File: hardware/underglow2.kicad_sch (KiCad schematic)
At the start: 1 part, among them J101 J_Delphi_Sicma_24

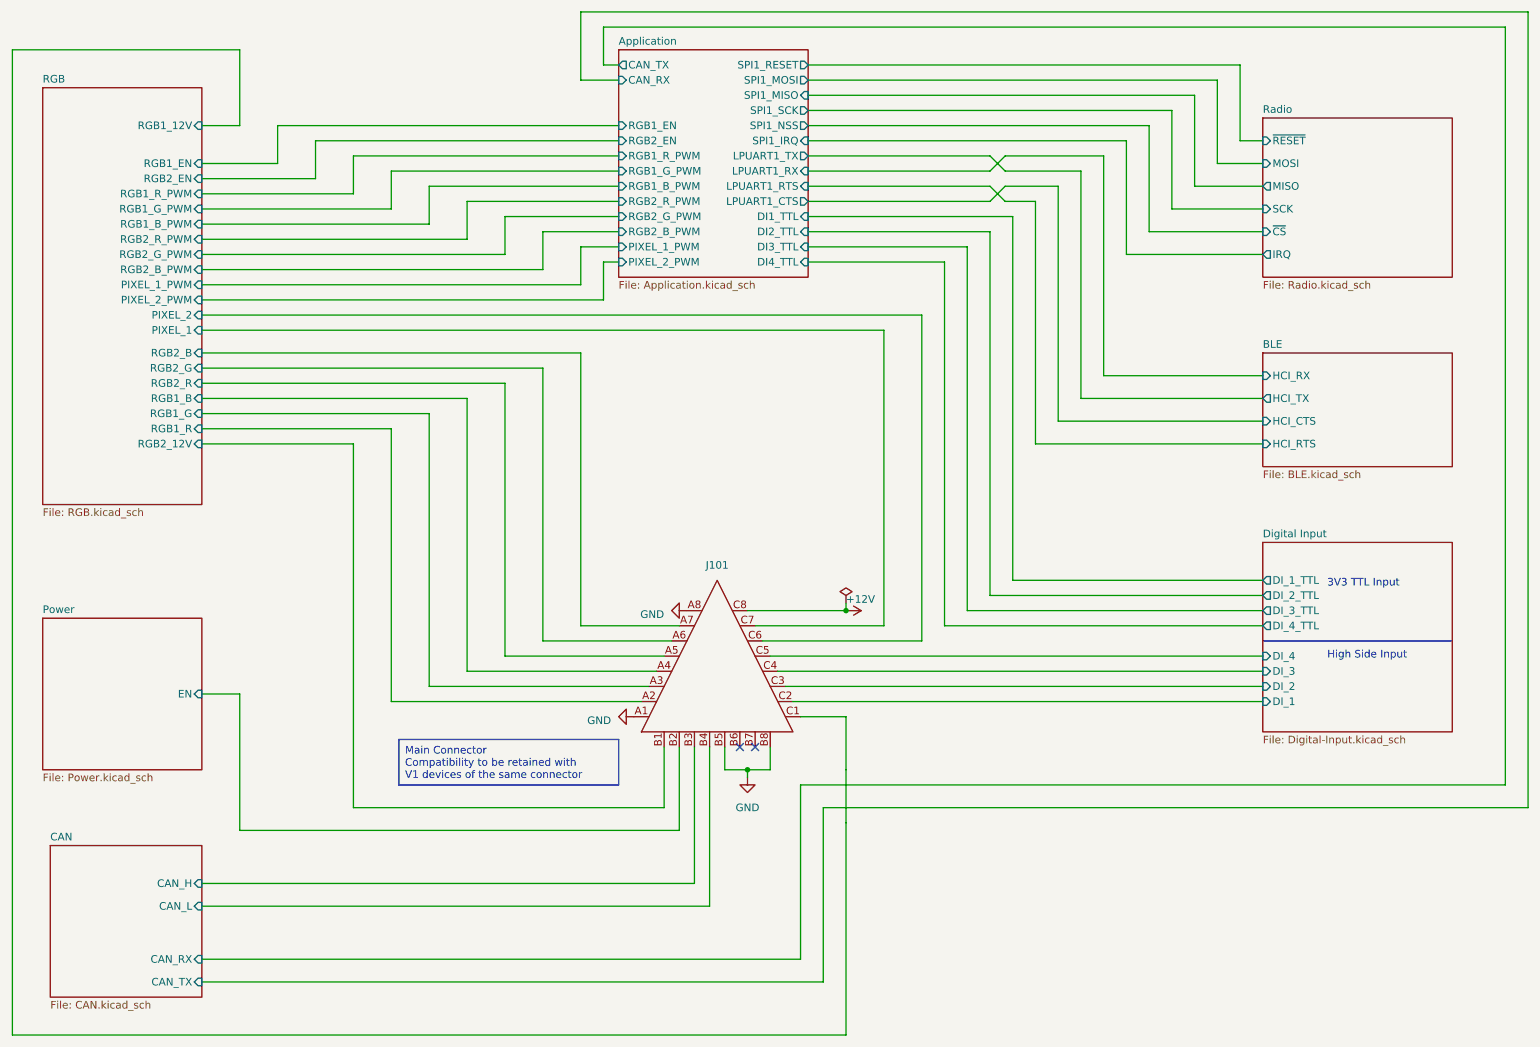
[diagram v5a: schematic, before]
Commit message: More pre-production updates:
* fix USART connections being reversed
* add test points for SPI and BLE

Signed-off-by: Connor Rigby <connorr@hey.com>
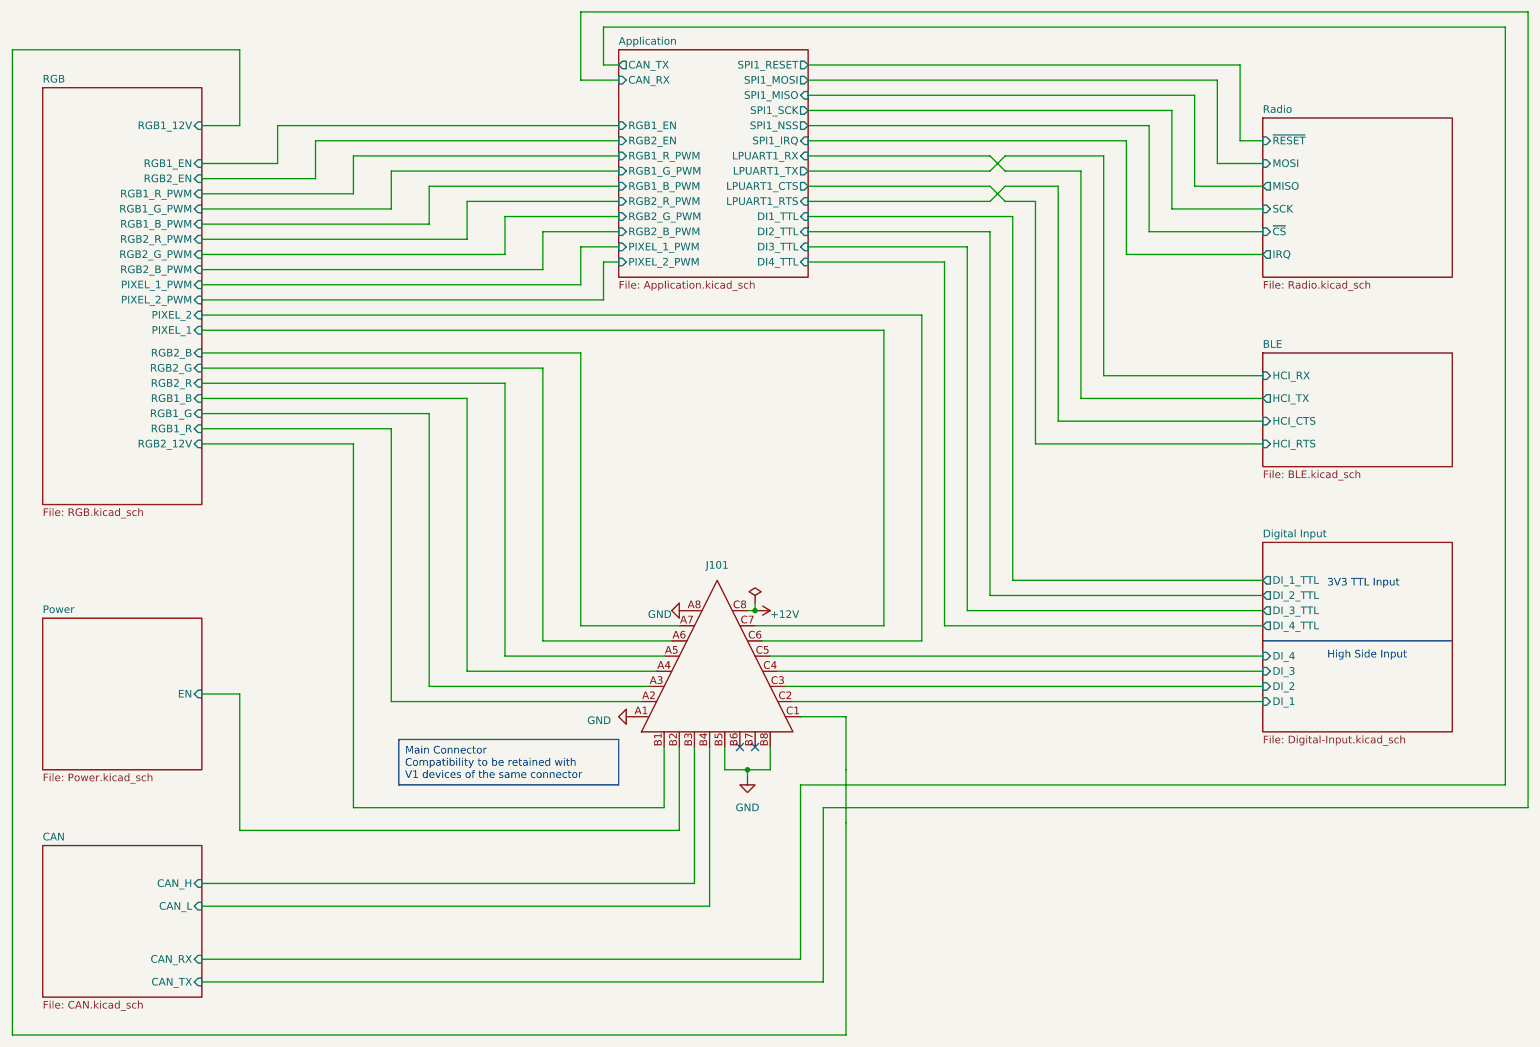
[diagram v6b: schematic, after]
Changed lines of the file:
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@@
   (junction (at 148.59 146.05) (diameter 0) (color 0 0 0 0)
   )
-  (junction (at 165.1 119.38) (diameter 0) (color 0 0 0 0)
+  (junction (at 149.86 119.38) (diameter 0) (color 0 0 0 0)
   )
   (no_connect (at 147.32 142.24))
@@
     (stroke (width 0) (type default))
   )
+  (wire (pts (xy 149.86 119.38) (xy 148.59 119.38))
+    (stroke (width 0) (type default))
+  )
   (wire (pts (xy 204.47 45.72) (xy 204.47 83.82))
     (stroke (width 0) (type default))
@@
     (stroke (width 0) (type default))
   )
-  (wire (pts (xy 165.1 118.11) (xy 165.1 119.38))
+  (wire (pts (xy 149.86 118.11) (xy 149.86 119.38))
     (stroke (width 0) (type default))
   )
@@
   )
   (wire (pts (xy 63.5 133.35) (xy 63.5 156.21))
-    (stroke (width 0) (type default))
-  )
-  (wire (pts (xy 165.1 119.38) (xy 148.59 119.38))
     (stroke (width 0) (type default))
   )
@@
   )
   (symbol (lib_id "power:GND") (at 138.43 119.38 270) (unit 1)
-    (in_bom yes) (on_board yes) (dnp no) (fields_autoplaced)
+    (in_bom yes) (on_board yes) (dnp no)
     (property "Reference" "#PWR0159" (at 132.08 119.38 0)
       (effects (font (size 1.27 1.27)) hide)
     )
-    (property "Value" "GND" (at 134.62 120.015 90)
+    (property "Value" "GND" (at 135.89 120.015 90)
       (effects (font (size 1.27 1.27)) (justify right))
     )
@@
     )
   )
-  (symbol (lib_id "power:PWR_FLAG") (at 165.1 118.11 0) (unit 1)
+  (symbol (lib_id "power:PWR_FLAG") (at 149.86 118.11 0) (unit 1)
     (in_bom yes) (on_board yes) (dnp no)
-    (property "Reference" "#FLG0105" (at 165.1 116.205 0)
-      (effects (font (size 1.27 1.27)) hide)
-    )
-    (property "Value" "PWR_FLAG" (at 165.1 114.3 0)
-      (effects (font (size 1.27 1.27)) hide)
-    )
-    (property "Footprint" "" (at 165.1 118.11 0)
-      (effects (font (size 1.27 1.27)) hide)
-    )
-    (property "Datasheet" "~" (at 165.1 118.11 0)
+    (property "Reference" "#FLG0105" (at 149.86 116.205 0)
+      (effects (font (size 1.27 1.27)) hide)
+    )
+    (property "Value" "PWR_FLAG" (at 149.86 114.3 0)
+      (effects (font (size 1.27 1.27)) hide)
+    )
+    (property "Footprint" "" (at 149.86 118.11 0)
+      (effects (font (size 1.27 1.27)) hide)
+    )
+    (property "Datasheet" "~" (at 149.86 118.11 0)
       (effects (font (size 1.27 1.27)) hide)
     )
@@
     )
   )
-  (symbol (lib_id "power:+12V") (at 165.1 119.38 270) (unit 1)
-    (in_bom yes) (on_board yes) (dnp no) (fields_autoplaced)
-    (property "Reference" "#PWR0107" (at 161.29 119.38 0)
-      (effects (font (size 1.27 1.27)) hide)
-    )
-    (property "Value" "+12V" (at 165.1 117.475 90)
-      (effects (font (size 1.27 1.27)) (justify left))
-    )
-    (property "Footprint" "" (at 165.1 119.38 0)
-      (effects (font (size 1.27 1.27)) hide)
-    )
-    (property "Datasheet" "" (at 165.1 119.38 0)
+  (symbol (lib_id "power:+12V") (at 149.86 119.38 270) (unit 1)
+    (in_bom yes) (on_board yes) (dnp no)
+    (property "Reference" "#PWR0107" (at 146.05 119.38 0)
+      (effects (font (size 1.27 1.27)) hide)
+    )
+    (property "Value" "+12V" (at 152.4 120.015 90)
+      (effects (font (size 1.27 1.27)) (justify left))
+    )
+    (property "Footprint" "" (at 149.86 119.38 0)
+      (effects (font (size 1.27 1.27)) hide)
+    )
+    (property "Datasheet" "" (at 149.86 119.38 0)
       (effects (font (size 1.27 1.27)) hide)
     )
@@
     )
   )
-  (sheet (at 31.75 158.75) (size 25.4 25.4) (fields_autoplaced)
+  (sheet (at 30.48 158.75) (size 26.67 25.4) (fields_autoplaced)
     (stroke (width 0.1524) (type solid))
     (fill (color 0 0 0 0.0000))
-    (property "Sheetname" "CAN" (at 31.75 158.0384 0)
+    (property "Sheetname" "CAN" (at 30.48 158.0384 0)
       (effects (font (size 1.27 1.27)) (justify left bottom))
     )
-    (property "Sheetfile" "CAN.kicad_sch" (at 31.75 184.7346 0)
+    (property "Sheetfile" "CAN.kicad_sch" (at 30.48 184.7346 0)
       (effects (font (size 1.27 1.27)) (justify left top))
     )
@@
       (effects (font (size 1.27 1.27)) (justify left))
     )
-    (pin "LPUART1_TX" output (at 158.75 43.18 0)
-      (effects (font (size 1.27 1.27)) (justify right))
-    )
-    (pin "LPUART1_RX" input (at 158.75 45.72 0)
-      (effects (font (size 1.27 1.27)) (justify right))
-    )
-    (pin "LPUART1_RTS" input (at 158.75 48.26 0)
-      (effects (font (size 1.27 1.27)) (justify right))
-    )
-    (pin "LPUART1_CTS" output (at 158.75 50.8 0)
-      (effects (font (size 1.27 1.27)) (justify right))
-    )
+    (pin "LPUART1_TX" output (at 158.75 45.72 0)
+      (effects (font (size 1.27 1.27)) (justify right))
+    )
+    (pin "LPUART1_RX" input (at 158.75 43.18 0)
+      (effects (font (size 1.27 1.27)) (justify right))
+    )
+    (pin "LPUART1_RTS" input (at 158.75 50.8 0)
+      (effects (font (size 1.27 1.27)) (justify right))
+    )
+    (pin "LPUART1_CTS" output (at 158.75 48.26 0)
+      (effects (font (size 1.27 1.27)) (justify right))
+    )

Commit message: Submitted for production
Signed-off-by: Connor Rigby <connorr@hey.com>
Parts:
- J101: Aliexpress (none) -> https://www.aliexpress.us/item/2251832669817996.html
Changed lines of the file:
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@@
+      (effects (font (size 1.27 1.27)) hide)
+    )
+    (property "Aliexpress" "https://www.aliexpress.us/item/2251832669817996.html" (at 143.51 127 0)
       (effects (font (size 1.27 1.27)) hide)
     )

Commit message: Rev 2 submitted for production
Signed-off-by: Connor Rigby <connorr@hey.com>
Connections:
- net RGB/PIXEL_1: now also J101.C6; no longer J101.C7
- net RGB/PIXEL_2: now also J101.C7; no longer J101.C6
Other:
- sheet Application ports: added CH1_B_PWM, CH1_EN_PWM, CH1_G_PWM, CH1_NZR, CH1_R_PWM, CH2_B_PWM, CH2_EN_PWM, CH2_G_PWM, CH2_NZR, CH2_R_PWM, HCI_CTS, HCI_EN, HCI_RTS, HCI_RX, HCI_TX, PI1, PI2, PI3, PI4, RADIO_IRQ, RADIO_MISO, RADIO_MOSI, RADIO_NSS, RADIO_SCK, ~{RADIO_RESET}; removed DI1_TTL, DI2_TTL, DI3_TTL, DI4_TTL, LPUART1_CTS, LPUART1_RTS, LPUART1_RX, LPUART1_TX, PIXEL_1_PWM, PIXEL_2_PWM, RGB1_B_PWM, RGB1_EN, RGB1_G_PWM, RGB1_R_PWM, RGB2_B_PWM, RGB2_EN, RGB2_G_PWM, RGB2_R_PWM, SPI1_IRQ, SPI1_MISO, SPI1_MOSI, SPI1_NSS, SPI1_RESET, SPI1_SCK
- sheet BLE ports: added HCI_EN; removed none
- sheet Digital Input ports: added PI1, PI2, PI3, PI4; removed DI_1_TTL, DI_2_TTL, DI_3_TTL, DI_4_TTL
- sheet RGB ports: added CH1_B_PWM, CH1_EN_PWM, CH1_G_PWM, CH1_NZR, CH1_R_PWM, CH2_B_PWM, CH2_EN_PWM, CH2_G_PWM, CH2_NZR, CH2_R_PWM; removed PIXEL_1_PWM, PIXEL_2_PWM, RGB1_B_PWM, RGB1_EN, RGB1_G_PWM, RGB1_R_PWM, RGB2_B_PWM, RGB2_EN, RGB2_G_PWM, RGB2_R_PWM
